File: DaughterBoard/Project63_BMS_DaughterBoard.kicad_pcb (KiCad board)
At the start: 2 copper layers, 71 parts, among them J1 705550019, U1 BQ79614PAPRQ1

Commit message: modhy commit
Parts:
- added C40: 0.22, Capacitor_SMD:C_1206_3216Metric, F.Cu at (70.2, -78.2)
- added Q1: 2n2222, OptoDevice:Osram_SFH3710, F.Cu at (75.5, -78.4)
- added R40: 100, Resistor_SMD:R_2010_5025Metric, F.Cu at (71.1, -86.2)
- added R41: 200, Resistor_SMD:R_2010_5025Metric, F.Cu at (71.1, -82.0)
- added TP1: ~, TestPoint:TestPoint_Keystone_5010-5014_Multipurpose, F.Cu at (52.8, -113.0)
- added TP10: ~, TestPoint:TestPoint_Keystone_5010-5014_Multipurpose, F.Cu at (57.8, -97.8)
- added TP11: ~, TestPoint:TestPoint_Keystone_5010-5014_Multipurpose, F.Cu at (57.8, -92.8)
- added TP12: ~, TestPoint:TestPoint_Keystone_5010-5014_Multipurpose, F.Cu at (57.8, -87.8)
- added TP13: ~, TestPoint:TestPoint_Keystone_5010-5014_Multipurpose, F.Cu at (62.9, -113.0)
- added TP14: ~, TestPoint:TestPoint_Keystone_5010-5014_Multipurpose, F.Cu at (62.9, -108.0)
- added TP15: ~, TestPoint:TestPoint_Keystone_5010-5014_Multipurpose, F.Cu at (62.9, -102.9)
- added TP16: ~, TestPoint:TestPoint_Keystone_5010-5014_Multipurpose, F.Cu at (62.9, -97.8)
- added TP17: ~, TestPoint:TestPoint_Keystone_5010-5014_Multipurpose, F.Cu at (62.9, -92.8)
- added TP18: Cell 10, TestPoint:TestPoint_Keystone_5010-5014_Multipurpose, F.Cu at (69.9, -113.0)
- added TP19: Cell 9, TestPoint:TestPoint_Keystone_5010-5014_Multipurpose, F.Cu at (69.9, -108.0)
- added TP2: ~, TestPoint:TestPoint_Keystone_5010-5014_Multipurpose, F.Cu at (52.8, -108.0)
- added TP20: Cell 8, TestPoint:TestPoint_Keystone_5010-5014_Multipurpose, F.Cu at (69.9, -102.9)
- added TP22: Cell 6, TestPoint:TestPoint_Keystone_5010-5014_Multipurpose, F.Cu at (69.9, -97.8)
- added TP23: Cell 5, TestPoint:TestPoint_Keystone_5010-5014_Multipurpose, F.Cu at (69.9, -92.8)
- added TP24: Cell 4, TestPoint:TestPoint_Keystone_5010-5014_Multipurpose, F.Cu at (75.0, -113.0)
- added TP25: Cell 3, TestPoint:TestPoint_Keystone_5010-5014_Multipurpose, F.Cu at (75.0, -108.0)
- added TP26: Cell 2, TestPoint:TestPoint_Keystone_5010-5014_Multipurpose, F.Cu at (75.0, -102.9)
- added TP27: Cell 1, TestPoint:TestPoint_Keystone_5010-5014_Multipurpose, F.Cu at (75.0, -97.8)
- added TP28: Cell 0S, TestPoint:TestPoint_Keystone_5010-5014_Multipurpose, F.Cu at (75.0, -92.8)
- added TP29: Cell 14, TestPoint:TestPoint_Keystone_5010-5014_Multipurpose, F.Cu at (80.0, -113.0)
- added TP3: ~, TestPoint:TestPoint_Keystone_5010-5014_Multipurpose, F.Cu at (52.8, -102.9)
- added TP30: Cell 13, TestPoint:TestPoint_Keystone_5010-5014_Multipurpose, F.Cu at (80.0, -108.0)
- added TP31: Cell 12, TestPoint:TestPoint_Keystone_5010-5014_Multipurpose, F.Cu at (80.0, -102.9)
- added TP32: Cell 11, TestPoint:TestPoint_Keystone_5010-5014_Multipurpose, F.Cu at (80.0, -97.8)
- added TP4: ~, TestPoint:TestPoint_Keystone_5010-5014_Multipurpose, F.Cu at (52.8, -97.8)
- added TP5: ~, TestPoint:TestPoint_Keystone_5010-5014_Multipurpose, F.Cu at (52.8, -92.8)
- added TP6: ~, TestPoint:TestPoint_Keystone_5010-5014_Multipurpose, F.Cu at (52.8, -87.8)
- added TP7: ~, TestPoint:TestPoint_Keystone_5010-5014_Multipurpose, F.Cu at (57.8, -113.0)
- added TP8: ~, TestPoint:TestPoint_Keystone_5010-5014_Multipurpose, F.Cu at (57.8, -108.0)
- added TP9: ~, TestPoint:TestPoint_Keystone_5010-5014_Multipurpose, F.Cu at (57.8, -102.9)
- C10: renamed from C19; footprint GCM188R71C474KA55D:G-188_MUR-L -> Capacitor_SMD:C_0201_0603Metric
- C11: renamed from C17; footprint GCM188R71C474KA55D:G-188_MUR-L -> Capacitor_SMD:C_0201_0603Metric
- C12: renamed from C15; footprint GCM188R71C474KA55D:G-188_MUR-L -> Capacitor_SMD:C_0201_0603Metric
- C13: footprint GCM188R71C474KA55D:G-188_MUR-L -> Capacitor_SMD:C_0201_0603Metric
- C14: renamed from C11; footprint GCM188R71C474KA55D:G-188_MUR-L -> Capacitor_SMD:C_0201_0603Metric
- C15: renamed from C9; footprint GCM188R71C474KA55D:G-188_MUR-L -> Capacitor_SMD:C_0201_0603Metric
- C16: renamed from C7; footprint GCM188R71C474KA55D:G-188_MUR-L -> Capacitor_SMD:C_0201_0603Metric
- C17: renamed from C5; footprint GCM188R71C474KA55D:G-188_MUR-L -> Capacitor_SMD:C_0201_0603Metric
- C18: renamed from C3; footprint GCM188R71C474KA55D:G-188_MUR-L -> Capacitor_SMD:C_0201_0603Metric
- C19: renamed from C1; footprint GCM188R71C474KA55D:G-188_MUR-L -> Capacitor_SMD:C_0201_0603Metric
- C20: renamed from C22; footprint GCM188R71C474KA55D:G-188_MUR-L -> Capacitor_SMD:C_0201_0603Metric
- C21: renamed from C20; footprint GCM188R71C474KA55D:G-188_MUR-L -> Capacitor_SMD:C_0201_0603Metric
- C22: renamed from C18; footprint GCM188R71C474KA55D:G-188_MUR-L -> Capacitor_SMD:C_0201_0603Metric
- C23: renamed from C16; footprint GCM188R71C474KA55D:G-188_MUR-L -> Capacitor_SMD:C_0201_0603Metric
- C24: renamed from C14; footprint GCM188R71C474KA55D:G-188_MUR-L -> Capacitor_SMD:C_0201_0603Metric
- C25: renamed from C12; footprint GCM188R71C474KA55D:G-188_MUR-L -> Capacitor_SMD:C_0201_0603Metric
- C26: renamed from C10; footprint GCM188R71C474KA55D:G-188_MUR-L -> Capacitor_SMD:C_0201_0603Metric
- C27: renamed from C8; footprint GCM188R71C474KA55D:G-188_MUR-L -> Capacitor_SMD:C_0201_0603Metric
- C28: renamed from C6; footprint GCM188R71C474KA55D:G-188_MUR-L -> Capacitor_SMD:C_0201_0603Metric
- C29: renamed from C4; footprint GCM188R71C474KA55D:G-188_MUR-L -> Capacitor_SMD:C_0201_0603Metric
- C30: renamed from C2; footprint GCM188R71C474KA55D:G-188_MUR-L -> Capacitor_SMD:C_0201_0603Metric
- C31: renamed from C29; footprint GCM188R71C474KA55D:G-188_MUR-L -> Capacitor_SMD:C_0201_0603Metric
- C32: renamed from C27; footprint GCM188R71C474KA55D:G-188_MUR-L -> Capacitor_SMD:C_0201_0603Metric
- C33: renamed from C25; footprint GCM188R71C474KA55D:G-188_MUR-L -> Capacitor_SMD:C_0201_0603Metric
- C34: renamed from C23; footprint GCM188R71C474KA55D:G-188_MUR-L -> Capacitor_SMD:C_0603_1608Metric
- C35: renamed from C30; footprint GCM188R71C474KA55D:G-188_MUR-L -> Capacitor_SMD:C_0201_0603Metric
- C36: renamed from C28; footprint GCM188R71C474KA55D:G-188_MUR-L -> Capacitor_SMD:C_0201_0603Metric
- C37: renamed from C26; footprint GCM188R71C474KA55D:G-188_MUR-L -> Capacitor_SMD:C_0201_0603Metric
- C38: renamed from C24; footprint GCM188R71C474KA55D:G-188_MUR-L -> Capacitor_SMD:C_0201_0603Metric
- C9: renamed from C21; footprint GCM188R71C474KA55D:G-188_MUR-L -> Capacitor_SMD:C_0201_0603Metric
- R10: renamed from R5; value 10 Ohm -> 7.5 Ohm; footprint CRCW121010R0FKEAHP:RC1210N_VIS-L -> Resistor_SMD:R_1206_3216Metric
- R11: renamed from R3; value 10 Ohm -> 7.5 Ohm; footprint CRCW121010R0FKEAHP:RC1210N_VIS-L -> Resistor_SMD:R_1206_3216Metric
- R12: renamed from R1; value 10 Ohm -> 7.5 Ohm; footprint CRCW121010R0FKEAHP:RC1210N_VIS-L -> Resistor_SMD:R_1206_3216Metric
- R13: renamed from R22; footprint ERA-3AEB101V:RC0603N_PAN-L -> Resistor_SMD:R_0201_0603Metric
- R14: renamed from R20; footprint ERA-3AEB101V:RC0603N_PAN-L -> Resistor_SMD:R_0201_0603Metric
- R15: renamed from R18; footprint ERA-3AEB101V:RC0603N_PAN-L -> Resistor_SMD:R_0201_0603Metric
- R16: footprint ERA-3AEB101V:RC0603N_PAN-L -> Resistor_SMD:R_0201_0603Metric
- R17: renamed from R14; footprint ERA-3AEB101V:RC0603N_PAN-L -> Resistor_SMD:R_0201_0603Metric
- R18: renamed from R12; footprint ERA-3AEB101V:RC0603N_PAN-L -> Resistor_SMD:R_0201_0603Metric
- R19: renamed from R10; footprint ERA-3AEB101V:RC0603N_PAN-L -> Resistor_SMD:R_0201_0603Metric
- R2: renamed from R21; value 10 Ohm -> 7.5 Ohm; footprint CRCW121010R0FKEAHP:RC1210N_VIS-L -> Resistor_SMD:R_1206_3216Metric
- R20: renamed from R8; footprint ERA-3AEB101V:RC0603N_PAN-L -> Resistor_SMD:R_0201_0603Metric
- R21: renamed from R6; footprint ERA-3AEB101V:RC0603N_PAN-L -> Resistor_SMD:R_0201_0603Metric
- R22: renamed from R4; footprint ERA-3AEB101V:RC0603N_PAN-L -> Resistor_SMD:R_0201_0603Metric
- R23: renamed from R2; footprint ERA-3AEB101V:RC0603N_PAN-L -> Resistor_SMD:R_0201_0603Metric
- R24: renamed from R29; value 10 Ohm -> 7.5 Ohm; footprint CRCW121010R0FKEAHP:RC1210N_VIS-L -> Resistor_SMD:R_1206_3216Metric
- R25: renamed from R27; value 10 Ohm -> 7.5 Ohm; footprint CRCW121010R0FKEAHP:RC1210N_VIS-L -> Resistor_SMD:R_1206_3216Metric
- R26: renamed from R25; value 10 Ohm -> 7.5 Ohm; footprint CRCW121010R0FKEAHP:RC1210N_VIS-L -> Resistor_SMD:R_1206_3216Metric
- R27: renamed from R23; value 10 Ohm -> 7.5 Ohm; footprint CRCW121010R0FKEAHP:RC1210N_VIS-L -> Resistor_SMD:R_1206_3216Metric
- R28: renamed from R30; footprint ERA-3AEB101V:RC0603N_PAN-L -> Resistor_SMD:R_0201_0603Metric
- R29: renamed from R28; footprint ERA-3AEB101V:RC0603N_PAN-L -> Resistor_SMD:R_0201_0603Metric
- R3: renamed from R19; value 10 Ohm -> 7.5 Ohm; footprint CRCW121010R0FKEAHP:RC1210N_VIS-L -> Resistor_SMD:R_1206_3216Metric
- R30: renamed from R26; footprint ERA-3AEB101V:RC0603N_PAN-L -> Resistor_SMD:R_0201_0603Metric
- R31: renamed from R24; footprint ERA-3AEB101V:RC0603N_PAN-L -> Resistor_SMD:R_0201_0603Metric
- R4: renamed from R17; value 10 Ohm -> 7.5 Ohm; footprint CRCW121010R0FKEAHP:RC1210N_VIS-L -> Resistor_SMD:R_1206_3216Metric
- R5: renamed from R15; value 10 Ohm -> 7.5 Ohm; footprint CRCW121010R0FKEAHP:RC1210N_VIS-L -> Resistor_SMD:R_1206_3216Metric
- R6: renamed from R13; value 10 Ohm -> 7.5 Ohm; footprint CRCW121010R0FKEAHP:RC1210N_VIS-L -> Resistor_SMD:R_1206_3216Metric
- R7: renamed from R11; value 10 Ohm -> 7.5 Ohm
- R8: renamed from R9; value 10 Ohm -> 7.5 Ohm; footprint CRCW121010R0FKEAHP:RC1210N_VIS-L -> Resistor_SMD:R_1206_3216Metric
- renumbered C31 to C1, C33 to C2, C36 to C3, C35 to C4, C32 to C5, C38 to C6, C37 to C7, C34 to C8, R31 to R1, R7 to R9
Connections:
- C6 pad 1: unconnected-(C38-Pad1) -> GND_CVSS
- U1 pad 52: unconnected-(U1-Pad52) -> CVDD
- U1 pad 63: unconnected-(U1-Pad63) -> /BQ79614_Bootstrapping/BBN
- U1 pad 64: unconnected-(U1-Pad64) -> /BQ79614_Bootstrapping/BBP

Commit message: 90% DOBO is done
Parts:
- removed C40: 0.22, Capacitor_SMD:C_1206_3216Metric
- removed Q1: 2n2222, OptoDevice:Osram_SFH3710
- removed R40: 100, Resistor_SMD:R_2010_5025Metric
- removed R41: 200, Resistor_SMD:R_2010_5025Metric
- removed the TP1 at (52.8, -113.0)
- removed the TP10 at (57.8, -97.8)
- removed the TP11 at (57.8, -92.8)
- removed the TP12 at (57.8, -87.8)
- removed the TP13 at (62.9, -113.0)
- removed the TP14 at (62.9, -108.0)
- removed the TP2 at (52.8, -108.0)
- removed the TP3 at (52.8, -102.9)
- removed the TP4 at (52.8, -97.8)
- removed the TP5 at (52.8, -92.8)
- removed the TP6 at (52.8, -87.8)
- removed the TP7 at (57.8, -113.0)
- removed the TP8 at (57.8, -108.0)
- removed the TP9 at (57.8, -102.9)
- added TP1: 5012, TP5012:TP_5012, F.Cu at (142.6, -89.0)
- added TP1: ~, TestPoint:TestPoint_Keystone_5010-5014_Multipurpose, F.Cu at (168.9, -90.2)
- added TP10: ~, TestPoint:TestPoint_Keystone_5010-5014_Multipurpose, F.Cu at (174.0, -75.0)
- added TP10: 5012, TP5012:TP_5012, F.Cu at (147.3, -70.1)
- added TP11: ~, TestPoint:TestPoint_Keystone_5010-5014_Multipurpose, F.Cu at (174.0, -70.0)
- added TP11: 5012, TP5012:TP_5012, F.Cu at (152.0, -89.0)
- added TP12: 5012, TP5012:TP_5012, F.Cu at (152.0, -84.3)
- added TP12: ~, TestPoint:TestPoint_Keystone_5010-5014_Multipurpose, F.Cu at (174.0, -64.9)
- added TP13: ~, TestPoint:TestPoint_Keystone_5010-5014_Multipurpose, F.Cu at (179.1, -90.2)
- added TP13: 5012, TP5012:TP_5012, F.Cu at (152.0, -79.6)
- added TP14: ~, TestPoint:TestPoint_Keystone_5010-5014_Multipurpose, F.Cu at (179.1, -85.1)
- added TP14: 5012, TP5012:TP_5012, F.Cu at (152.0, -74.8)
- added TP2: 5012, TP5012:TP_5012, F.Cu at (142.6, -84.3)
- added TP2: ~, TestPoint:TestPoint_Keystone_5010-5014_Multipurpose, F.Cu at (168.9, -85.1)
- added TP21: 5012, TP5012:TP_5012, F.Cu at (201.1, -79.5)
- added TP3: 5012, TP5012:TP_5012, F.Cu at (142.6, -79.6)
- added TP3: ~, TestPoint:TestPoint_Keystone_5010-5014_Multipurpose, F.Cu at (168.9, -80.0)
- added TP4: 5012, TP5012:TP_5012, F.Cu at (142.6, -74.8)
- added TP4: ~, TestPoint:TestPoint_Keystone_5010-5014_Multipurpose, F.Cu at (168.9, -75.0)
- added TP5: 5012, TP5012:TP_5012, F.Cu at (142.6, -70.1)
- added TP5: ~, TestPoint:TestPoint_Keystone_5010-5014_Multipurpose, F.Cu at (168.9, -70.0)
- added TP6: ~, TestPoint:TestPoint_Keystone_5010-5014_Multipurpose, F.Cu at (168.9, -64.9)
- added TP6: 5012, TP5012:TP_5012, F.Cu at (147.3, -89.0)
- added TP7: ~, TestPoint:TestPoint_Keystone_5010-5014_Multipurpose, F.Cu at (174.0, -90.2)
- added TP7: 5012, TP5012:TP_5012, F.Cu at (147.3, -84.3)
- added TP8: ~, TestPoint:TestPoint_Keystone_5010-5014_Multipurpose, F.Cu at (174.0, -85.1)
- added TP8: 5012, TP5012:TP_5012, F.Cu at (147.3, -79.6)
- added TP9: ~, TestPoint:TestPoint_Keystone_5010-5014_Multipurpose, F.Cu at (174.0, -80.0)
- added TP9: 5012, TP5012:TP_5012, F.Cu at (147.3, -74.8)
- C10, C11, C12, C13, C14, C15, C16, C17, C18, C19, C20, C21, C22, C23, C24, C25, C26, C27, C28, C29, C30, C31, C32, C33, C35, C36, C37, C38, C9: footprint Capacitor_SMD:C_0201_0603Metric -> GCM188R71C474KA55D:G-188_MUR-L
- C34: footprint Capacitor_SMD:C_0603_1608Metric -> GCM188R71C474KA55D:G-188_MUR-L
- R10, R4, R5: value 7.5 Ohm -> 7.5 ohm; footprint Resistor_SMD:R_1206_3216Metric -> CRCW12067R50FKEAHP:RES_V1206_VIS-L
- R11, R12, R2, R24, R25, R26, R27, R3, R6, R8: footprint Resistor_SMD:R_1206_3216Metric -> CRCW12067R50FKEAHP:RES_V1206_VIS-L
- R13, R14, R15, R16, R17, R18, R19, R20, R21, R22, R23, R28, R29, R30, R31: footprint Resistor_SMD:R_0201_0603Metric -> ERA-3AEB101V:RC0603N_PAN-L
- R7: footprint CRCW121010R0FKEAHP:RC1210N_VIS-L -> CRCW12067R50FKEAHP:RES_V1206_VIS-L
- R9: value 10 Ohm -> 7.5 Ohm; footprint CRCW121010R0FKEAHP:RC1210N_VIS-L -> CRCW12067R50FKEAHP:RES_V1206_VIS-L
- TP18: value Cell 10 -> 5012; footprint TestPoint:TestPoint_Keystone_5010-5014_Multipurpose -> TP5012:TP_5012
- TP19: value Cell 9 -> 5012; footprint TestPoint:TestPoint_Keystone_5010-5014_Multipurpose -> TP5012:TP_5012
- TP20: value Cell 8 -> 5012; footprint TestPoint:TestPoint_Keystone_5010-5014_Multipurpose -> TP5012:TP_5012
- TP22: value Cell 6 -> 5012; footprint TestPoint:TestPoint_Keystone_5010-5014_Multipurpose -> TP5012:TP_5012
- TP23: value Cell 5 -> 5012; footprint TestPoint:TestPoint_Keystone_5010-5014_Multipurpose -> TP5012:TP_5012
- TP24: value Cell 4 -> 5012; footprint TestPoint:TestPoint_Keystone_5010-5014_Multipurpose -> TP5012:TP_5012
- TP25: value Cell 3 -> 5012; footprint TestPoint:TestPoint_Keystone_5010-5014_Multipurpose -> TP5012:TP_5012
- TP26: value Cell 2 -> 5012; footprint TestPoint:TestPoint_Keystone_5010-5014_Multipurpose -> TP5012:TP_5012
- TP27: value Cell 1 -> 5012; footprint TestPoint:TestPoint_Keystone_5010-5014_Multipurpose -> TP5012:TP_5012
- TP28: value Cell 0S -> 5012; footprint TestPoint:TestPoint_Keystone_5010-5014_Multipurpose -> TP5012:TP_5012
- TP29: value Cell 14 -> 5012; footprint TestPoint:TestPoint_Keystone_5010-5014_Multipurpose -> TP5012:TP_5012
- TP30: value Cell 13 -> 5012; footprint TestPoint:TestPoint_Keystone_5010-5014_Multipurpose -> TP5012:TP_5012
- TP31: value Cell 12 -> 5012; footprint TestPoint:TestPoint_Keystone_5010-5014_Multipurpose -> TP5012:TP_5012
- TP32: value Cell 11 -> 5011; footprint TestPoint:TestPoint_Keystone_5010-5014_Multipurpose -> 5011 (1):TP_5011
- moved TP18 151.4 mm to (213.0, -63.5)
- moved TP32 145.7 mm to (213.5, -39.5)
- moved TP22 133.2 mm to (201.1, -74.8)
- moved TP23 133.1 mm to (201.1, -70.1)
- moved TP24 133.0 mm to (205.8, -88.9)
- moved TP25 133.0 mm to (205.8, -84.2)
- moved TP26 132.9 mm to (205.8, -79.5)
- moved TP27 132.8 mm to (205.8, -74.8)
- moved TP28 132.8 mm to (205.8, -70.1)
- moved TP29 132.7 mm to (210.5, -88.9)
- moved TP30 132.6 mm to (210.5, -84.2)
- moved TP31 132.6 mm to (210.5, -79.5)
- moved TP19 132.5 mm to (201.1, -88.9)
- moved TP20 132.5 mm to (201.1, -84.2)
- moved TP15 118.4 mm to (179.1, -80.0)
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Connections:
- R24 pad 1: CB14 -> CB11
- R24 pad 2: Cell 14S -> Cell 11
- R25 pad 1: CB13 -> CB12
- R25 pad 2: Cell 13 -> Cell 12
- R26 pad 1: CB12 -> CB13
- R26 pad 2: Cell 12 -> Cell 13
- R27 pad 1: CB11 -> CB14
- R27 pad 2: Cell 11 -> Cell 14S
- U1 pad 63: /BQ79614_Bootstrapping/BBN -> unconnected-(U1-Pad63)
- U1 pad 64: /BQ79614_Bootstrapping/BBP -> unconnected-(U1-Pad64)

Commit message: NPN is done
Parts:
- added C39: 0.22µF, GCM31MR72A224KA3L:G-31_MUR-L, F.Cu at (62.1, -105.1)
- added Q1: ZXTN4004KTC, ZXTN4004KTC:ZXTN4004KTC, F.Cu at (54.0, -107.6)
- added R32: 100, CRCW2010100RFKEF:RES_CRCW_2010-L, F.Cu at (62.3, -112.5)
- added R33: 200, CRCW2010200RFKEF:RC2010N_VIS-L, F.Cu at (62.2, -108.5)

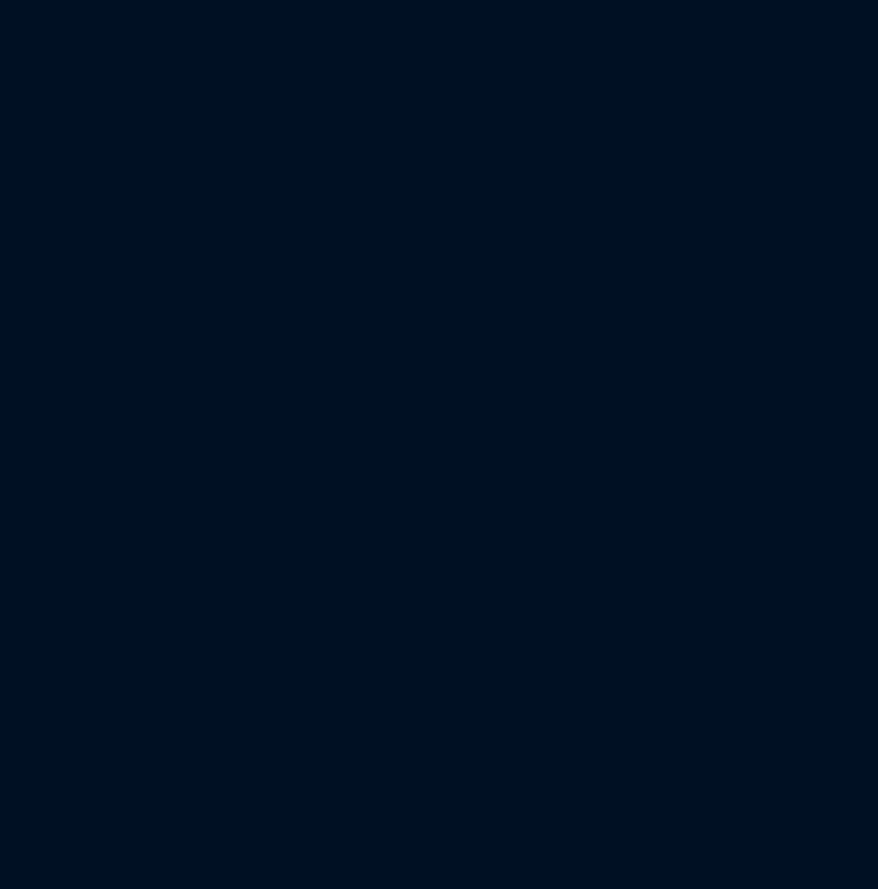
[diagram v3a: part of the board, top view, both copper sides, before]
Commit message: I think all componets for DOBO schematic are added, wired and assigned to their footprints. Next step to work on ERC
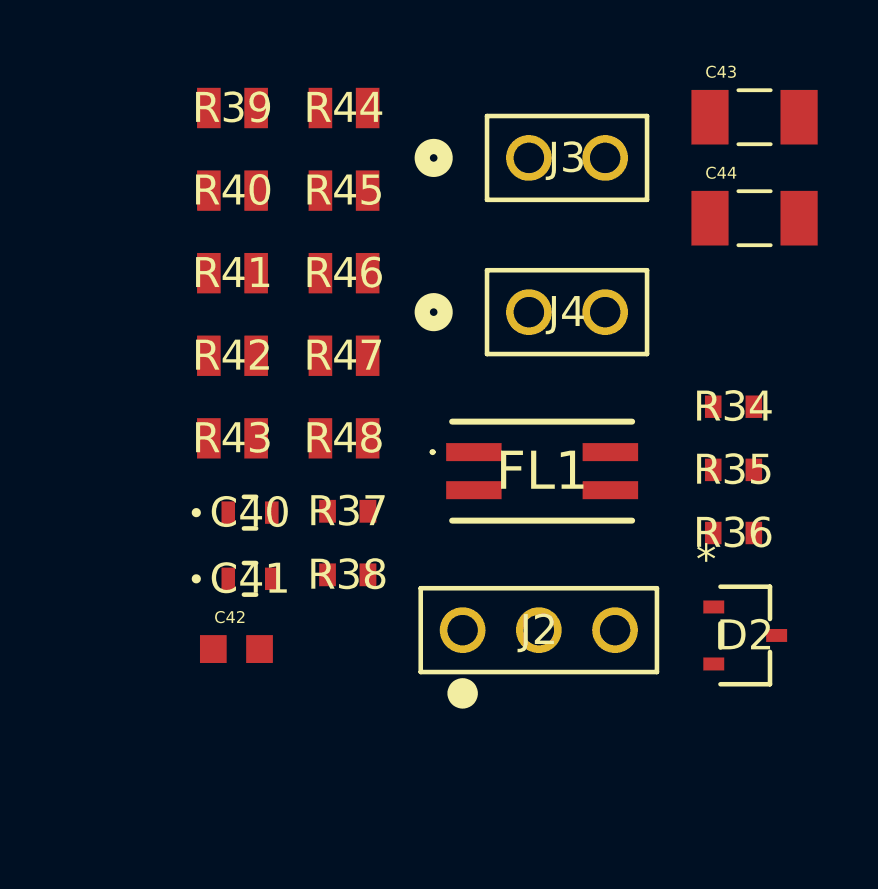
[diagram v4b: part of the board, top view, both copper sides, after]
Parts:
- added C40: 220pF, CL10B221JB8NNNC:CAP_CL10_SAM-L, F.Cu at (273.7, -130.3)
- added C41: 220pF, CL10B221JB8NNNC:CAP_CL10_SAM-L, F.Cu at (273.7, -128.1)
- added C42: 100pF, GCM1885C1H101JA16J (1):CAPC1608X90N, F.Cu at (273.2, -125.8)
- added C43: 2200pF, 1206J2K00222KXR (1):CAPC3216X160N, F.Cu at (290.5, -143.5)
- added C44: 2200pF, 1206J2K00222KXR (1):CAPC3216X160N, F.Cu at (290.5, -140.1)
- added D2: 24V, PESD1CAN,215:SOT23_PESD1_NEX-L, F.Cu at (290.2, -126.2)
- added FL1: 470uH, 744242471:744242471, F.Cu at (283.4, -131.7)
- added J2: PEC03SAAN, PEC03SAAN:CONN_PEC03SAAN_SUL, F.Cu at (280.8, -126.4)
- added J3: PEC02SAAN, PEC02SAAN:CONN_PxC02S_SUL, F.Cu at (283.0, -142.1)
- added J4: PEC02SAAN, PEC02SAAN:CONN_PxC02S_SUL, F.Cu at (283.0, -137.0)
- added R34: 51, CRCW060351R0JNEA:RC0603N_VIS-L, F.Cu at (289.8, -133.9)
- added R35: 51, CRCW060351R0JNEA:RC0603N_VIS-L, F.Cu at (289.8, -131.7)
- added R36: 1.00K, ERJ-3EKF1001V:RC0603N_PAN-L, F.Cu at (289.8, -129.6)
- added R37: 0, RC0603JR-070RL:RC0603N_YAG-L, F.Cu at (277.0, -130.4)
- added R38: 0, RC0603JR-070RL:RC0603N_YAG-L, F.Cu at (277.0, -128.2)
- added R39: 0, CRCW08050000Z0EAHP:RES_CRCW_0805_VIS-L, F.Cu at (273.1, -143.8)
- added R40: 0, CRCW08050000Z0EAHP:RES_CRCW_0805_VIS-L, F.Cu at (273.1, -141.1)
- added R41: 0, CRCW08050000Z0EAHP:RES_CRCW_0805_VIS-L, F.Cu at (273.1, -138.3)
- added R42: 0, CRCW08050000Z0EAHP:RES_CRCW_0805_VIS-L, F.Cu at (273.1, -135.5)
- added R43: 0, CRCW08050000Z0EAHP:RES_CRCW_0805_VIS-L, F.Cu at (273.1, -132.8)
- added R44: 0, CRCW08050000Z0EAHP:RES_CRCW_0805_VIS-L, F.Cu at (276.8, -143.8)
- added R45: 0, CRCW08050000Z0EAHP:RES_CRCW_0805_VIS-L, F.Cu at (276.8, -141.1)
- added R46: 0, CRCW08050000Z0EAHP:RES_CRCW_0805_VIS-L, F.Cu at (276.8, -138.3)
- added R47: 0, CRCW08050000Z0EAHP:RES_CRCW_0805_VIS-L, F.Cu at (276.8, -135.5)
- added R48: 0, CRCW08050000Z0EAHP:RES_CRCW_0805_VIS-L, F.Cu at (276.8, -132.8)

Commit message: ready for pcb
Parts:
- added C42: 220pF, CL10B221JB8NNNC:CAP_CL10_SAM, F.Cu at (192.6, -137.6)
- added C45: 220pF, CL10B221JB8NNNC:CAP_CL10_SAM, F.Cu at (192.6, -135.1)
- added D1: 24V, PESD1CAN,215:SOT23_PESD1_NEX, F.Cu at (197.0, -136.3)
- added FL2: 470uH, 744242471:744242471, F.Cu at (181.9, -135.6)
- added J2: 705510038, 70551-0038:CONN_70551-xxxx_04_MOL, F.Cu at (184.8, -152.5)
- added J3: 705510038, 70551-0038:CONN_70551-xxxx_04_MOL, F.Cu at (201.5, -152.5)
- added R39: 0, RC0603JR-070RL:RC0603N_YAG, F.Cu at (188.6, -137.6)
- added R40: 0, RC0603JR-070RL:RC0603N_YAG, F.Cu at (188.6, -135.1)
- added R41: 51, CRCW060351R0JNEA:RC0603N_VIS, F.Cu at (175.2, -137.6)
- added R42: 51, CRCW060351R0JNEA:RC0603N_VIS, F.Cu at (175.2, -135.1)
- added R49: 1.00K, ERA-3AEB101V:RC0603N_PAN, F.Cu at (175.2, -132.6)
- added R50: 0, CRCW08050000Z0EAHP:RES_CRCW_0805_VIS, F.Cu at (171.2, -154.1)
- added R51: 0, CRCW08050000Z0EAHP:RES_CRCW_0805_VIS, F.Cu at (171.2, -151.3)
- added R52: 0, CRCW08050000Z0EAHP:RES_CRCW_0805_VIS, F.Cu at (171.2, -148.5)
- added R53: 0, CRCW08050000Z0EAHP:RES_CRCW_0805_VIS, F.Cu at (171.2, -145.7)
- added R54: 0, CRCW08050000Z0EAHP:RES_CRCW_0805_VIS, F.Cu at (171.2, -142.9)
- added R55: 0, CRCW08050000Z0EAHP:RES_CRCW_0805_VIS, F.Cu at (171.2, -140.1)
- C39: footprint GCM31MR72A224KA3L:G-31_MUR-L -> GCM31MR72A224KA3L:G-31_MUR
- C40, C41: footprint CL10B221JB8NNNC:CAP_CL10_SAM-L -> CL10B221JB8NNNC:CAP_CL10_SAM
- D2: footprint PESD1CAN,215:SOT23_PESD1_NEX-L -> PESD1CAN,215:SOT23_PESD1_NEX
- R32: footprint CRCW2010100RFKEF:RES_CRCW_2010-L -> CRCW2010100RFKEF:RES_CRCW_2010
- R33: footprint CRCW2010200RFKEF:RC2010N_VIS-L -> CRCW2010200RFKEF:RC2010N_VIS
- R34, R35: footprint CRCW060351R0JNEA:RC0603N_VIS-L -> CRCW060351R0JNEA:RC0603N_VIS
- R36: footprint ERJ-3EKF1001V:RC0603N_PAN-L -> ERA-3AEB101V:RC0603N_PAN
- R37, R38: footprint RC0603JR-070RL:RC0603N_YAG-L -> RC0603JR-070RL:RC0603N_YAG
- R43, R44, R45, R46, R47, R48: footprint CRCW08050000Z0EAHP:RES_CRCW_0805_VIS-L -> CRCW08050000Z0EAHP:RES_CRCW_0805_VIS
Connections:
- C1 pad 1: GND_AVSS -> AVSS
- C19 pad 1: GND_AVSS -> AVSS
- C2 pad 1: GND_CVSS -> AVSS
- C3 pad 1: GND_REFHM -> AVSS
- C30 pad 1: GND_AVSS -> AVSS
- C4 pad 1: GND_AVSS -> AVSS
- C5 pad 1: GND_CVSS -> AVSS
- C6 pad 1: GND_CVSS -> AVSS
- C7 pad 1: GND_DVSS -> AVSS
- C8 pad 1: GND_CVSS -> AVSS
- D2 pad 2: Net-(D2-Pad1) -> Net-(D2-Pad2)
- R1 pad 2: PWR -> Cell 14S
- R33 pad 2: PWR -> Cell 14S
- R35 pad 2: Net-(D2-Pad1) -> Net-(D2-Pad2)
- R37 pad 2: Net-(D2-Pad1) -> Net-(D2-Pad2)
- U1 pad EPAD: AVSS -> unconnected-(U1-PadEPAD)
